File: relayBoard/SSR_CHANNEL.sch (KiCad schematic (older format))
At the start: 4 parts, among them K43 CPC1708J

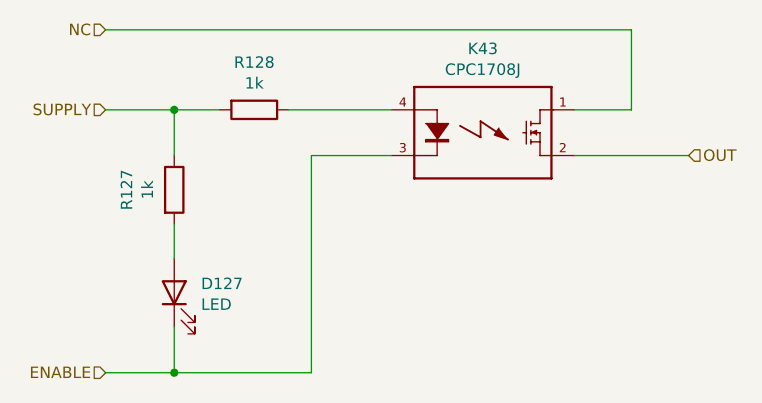
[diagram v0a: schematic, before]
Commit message: Third pass, fixing footprints to match JLC components
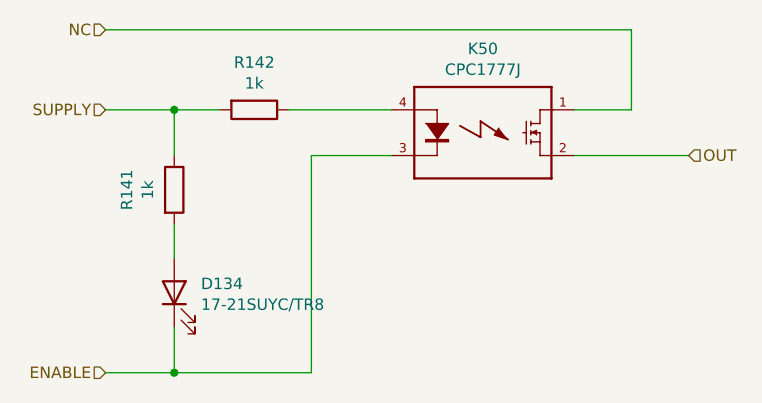
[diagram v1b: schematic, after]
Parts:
- D127: value LED -> 17-21SUYC/TR8
- K43: value CPC1708J -> CPC1777J
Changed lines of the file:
@@
 $Descr A4 11693 8268
 encoding utf-8
-Sheet 44 66
+Sheet 51 66
 Title ""
 Date ""
@@
 AR Path="/5F6754DE/5F4CB03A" Ref="R168"  Part="1"
 AR Path="/5F6754EA/5F4CB03A" Ref="R?"  Part="1"
-F 0 "R128" V 4143 3050 50  0000 C CNN
+F 0 "R142" V 4143 3050 50  0000 C CNN
 F 1 "1k" V 4234 3050 50  0000 C CNN
 F 2 "Resistor_SMD:R_0603_1608Metric" V 4280 3050 50  0001 C CNN
@@
 AR Path="/5F6754D2/63133440" Ref="K62"  Part="1"
 AR Path="/5F6754DE/63133440" Ref="K63"  Part="1"
-F 0 "K43" H 5350 3517 50  0000 C CNN
-F 1 "CPC1708J" H 5350 3426 50  0000 C CNN
+F 0 "K50" H 5350 3517 50  0000 C CNN
+F 1 "CPC1777J" H 5350 3426 50  0000 C CNN
 F 2 "TO381P2016X515X2916-4:TO381P2016X515X2916-4" H 5350 3150 50  0001 L BNN
 F 3 "" H 5350 3150 50  0001 C CNN
@@
 AR Path="/5F6754D2/5F3598FB" Ref="D146"  Part="1"
 AR Path="/5F6754DE/5F3598FB" Ref="D147"  Part="1"
-F 0 "D127" V 4039 3733 50  0000 R CNN
-F 1 "LED" V 3948 3733 50  0000 R CNN
+F 0 "D134" V 4039 3733 50  0000 R CNN
+F 1 "17-21SUYC/TR8" V 3948 3733 50  0000 R CNN
 F 2 "Resistor_SMD:R_0805_2012Metric" H 4000 3850 50  0001 C CNN
 F 3 "~" H 4000 3850 50  0001 C CNN
@@
 AR Path="/5F6754D2/5F359901" Ref="R165"  Part="1"
 AR Path="/5F6754DE/5F359901" Ref="R167"  Part="1"
-F 0 "R127" V 3793 3400 50  0000 C CNN
+F 0 "R141" V 3793 3400 50  0000 C CNN
 F 1 "1k" V 3884 3400 50  0000 C CNN
 F 2 "Resistor_SMD:R_0603_1608Metric" V 3930 3400 50  0001 C CNN

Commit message: Cuyler's revisions to the relay board
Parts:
- K43: symbol CPC1708J:CPC1708J -> relayBoard-rescue:CPC1708J-CPC1708J
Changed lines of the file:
@@
 EESchema Schematic File Version 4
-EELAYER 30 0
+LIBS:relayBoard-cache
+EELAYER 29 0
 EELAYER END
 $Descr A4 11693 8268
 encoding utf-8
-Sheet 51 66
+Sheet 48 66
 Title ""
 Date ""
@@
 AR Path="/5F6754DE/5F4CB03A" Ref="R168"  Part="1"
 AR Path="/5F6754EA/5F4CB03A" Ref="R?"  Part="1"
-F 0 "R142" V 4143 3050 50  0000 C CNN
+F 0 "R136" V 4143 3050 50  0000 C CNN
 F 1 "1k" V 4234 3050 50  0000 C CNN
 F 2 "Resistor_SMD:R_0603_1608Metric" V 4280 3050 50  0001 C CNN
@@
 OUT
 $Comp
-L CPC1708J:CPC1708J K43
+L relayBoard-rescue:CPC1708J-CPC1708J K43
 U 1 1 63133440
 P 5350 3150
@@
 AR Path="/5F6754D2/63133440" Ref="K62"  Part="1"
 AR Path="/5F6754DE/63133440" Ref="K63"  Part="1"
-F 0 "K50" H 5350 3517 50  0000 C CNN
+F 0 "K47" H 5350 3517 50  0000 C CNN
 F 1 "CPC1777J" H 5350 3426 50  0000 C CNN
 F 2 "TO381P2016X515X2916-4:TO381P2016X515X2916-4" H 5350 3150 50  0001 L BNN
@@
 AR Path="/5F6754D2/5F3598FB" Ref="D146"  Part="1"
 AR Path="/5F6754DE/5F3598FB" Ref="D147"  Part="1"
-F 0 "D134" V 4039 3733 50  0000 R CNN
+F 0 "D131" V 4039 3733 50  0000 R CNN
 F 1 "17-21SUYC/TR8" V 3948 3733 50  0000 R CNN
 F 2 "Resistor_SMD:R_0805_2012Metric" H 4000 3850 50  0001 C CNN
@@
 AR Path="/5F6754D2/5F359901" Ref="R165"  Part="1"
 AR Path="/5F6754DE/5F359901" Ref="R167"  Part="1"
-F 0 "R141" V 3793 3400 50  0000 C CNN
+F 0 "R135" V 3793 3400 50  0000 C CNN
 F 1 "1k" V 3884 3400 50  0000 C CNN
 F 2 "Resistor_SMD:R_0603_1608Metric" V 3930 3400 50  0001 C CNN

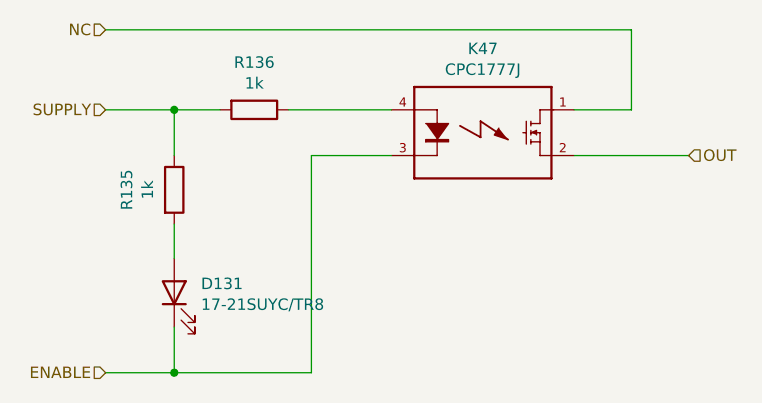
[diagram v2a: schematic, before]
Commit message: updates to connector connections and converter transformer
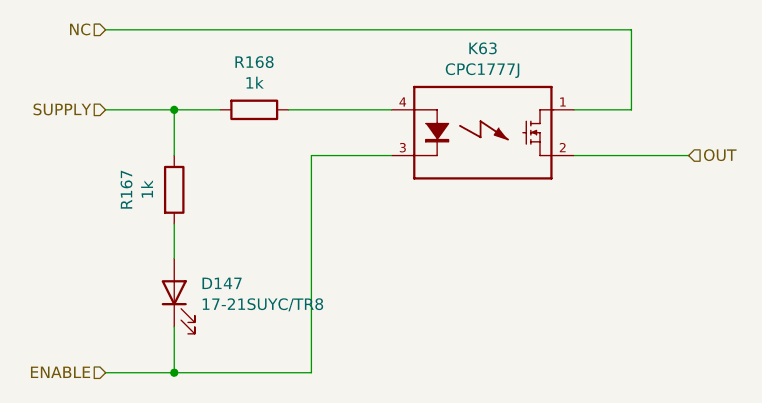
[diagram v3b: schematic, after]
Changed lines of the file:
@@
 EESchema Schematic File Version 4
-LIBS:relayBoard-cache
-EELAYER 29 0
+EELAYER 30 0
 EELAYER END
 $Descr A4 11693 8268
@@
 AR Path="/5F6754DE/5F4CB03A" Ref="R168"  Part="1"
 AR Path="/5F6754EA/5F4CB03A" Ref="R?"  Part="1"
-F 0 "R136" V 4143 3050 50  0000 C CNN
+F 0 "R168" V 4143 3050 50  0000 C CNN
 F 1 "1k" V 4234 3050 50  0000 C CNN
 F 2 "Resistor_SMD:R_0603_1608Metric" V 4280 3050 50  0001 C CNN
@@
 AR Path="/5F6754D2/63133440" Ref="K62"  Part="1"
 AR Path="/5F6754DE/63133440" Ref="K63"  Part="1"
-F 0 "K47" H 5350 3517 50  0000 C CNN
+F 0 "K63" H 5350 3517 50  0000 C CNN
 F 1 "CPC1777J" H 5350 3426 50  0000 C CNN
 F 2 "TO381P2016X515X2916-4:TO381P2016X515X2916-4" H 5350 3150 50  0001 L BNN
@@
 AR Path="/5F6754D2/5F3598FB" Ref="D146"  Part="1"
 AR Path="/5F6754DE/5F3598FB" Ref="D147"  Part="1"
-F 0 "D131" V 4039 3733 50  0000 R CNN
+F 0 "D147" V 4039 3733 50  0000 R CNN
 F 1 "17-21SUYC/TR8" V 3948 3733 50  0000 R CNN
 F 2 "Resistor_SMD:R_0805_2012Metric" H 4000 3850 50  0001 C CNN
@@
 AR Path="/5F6754D2/5F359901" Ref="R165"  Part="1"
 AR Path="/5F6754DE/5F359901" Ref="R167"  Part="1"
-F 0 "R135" V 3793 3400 50  0000 C CNN
+F 0 "R167" V 3793 3400 50  0000 C CNN
 F 1 "1k" V 3884 3400 50  0000 C CNN
 F 2 "Resistor_SMD:R_0603_1608Metric" V 3930 3400 50  0001 C CNN
